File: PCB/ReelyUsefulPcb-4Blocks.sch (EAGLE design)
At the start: 28 parts, among them Q1 200mA/50V, U2 TJCTM240, U3 PHOTON_SMD

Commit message: Updated notes.
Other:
- note added: "Actually photo-transistors (L-93DP3C) Short lead (Collector) goes to +ve"
- note removed: "Diodes need to be reversed"
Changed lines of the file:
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@@
 <wire x1="144.78" y1="2.54" x2="106.68" y2="2.54" width="0.1524" layer="97"/>
 <text x="63.5" y="43.18" size="1.27" layer="97">Hand held detector</text>
-<text x="25.4" y="48.26" size="1.27" layer="91">Diodes need to be reversed</text>
+<text x="25.4" y="48.26" size="1.27" layer="97">Actually photo-transistors (L-93DP3C)
+Short lead (Collector) goes to +ve</text>
 <text x="238.76" y="7.62" size="1.27" layer="97">1.0</text>
 <text x="170.942" y="11.684" size="1.27" layer="97">Stephen Harrison</text>

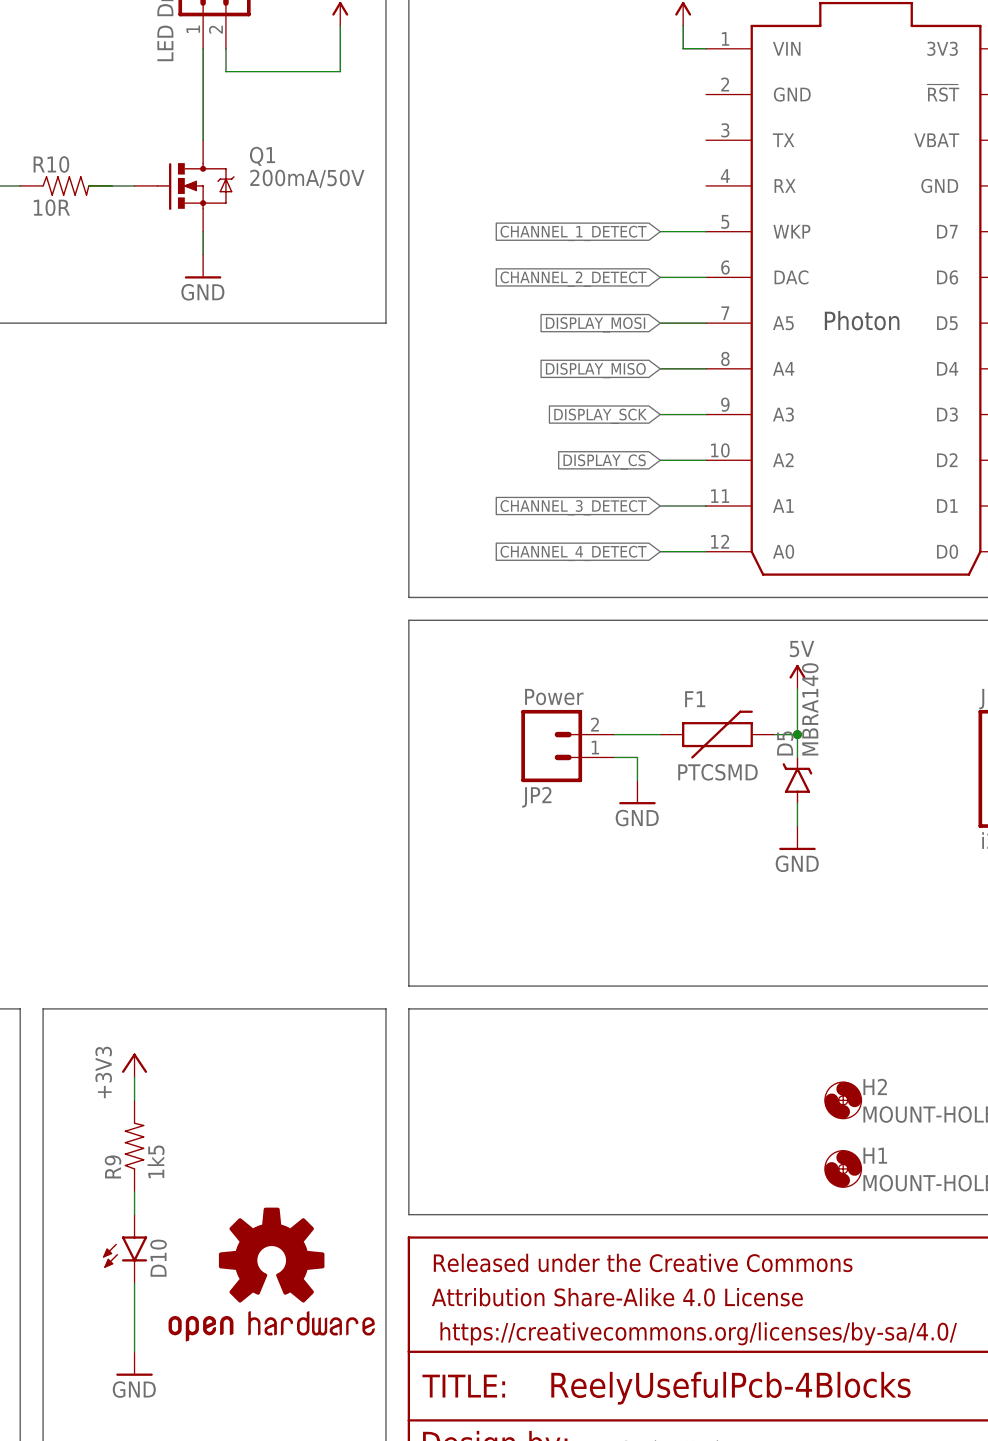
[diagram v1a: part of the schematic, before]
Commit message: Monior improvements to pcb/schematic names and values.
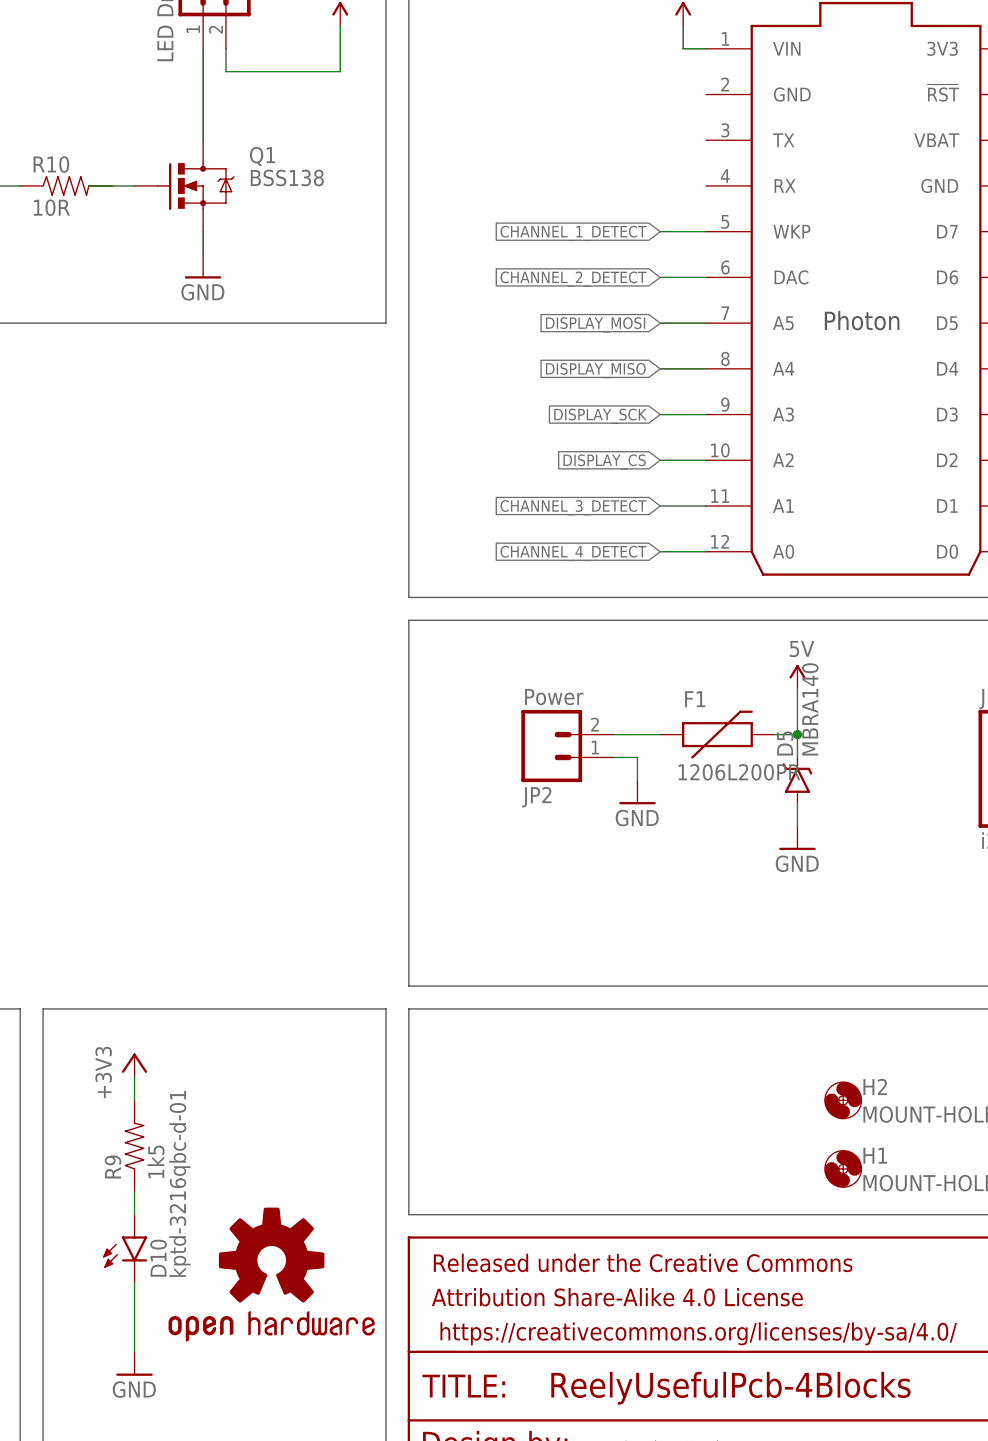
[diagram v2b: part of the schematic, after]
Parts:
- D10: value (none) -> kptd-3216qbc-d-01; FARNELL (none) -> 2290349
- F1: value PTCSMD -> 1206L200PR; FARNELL (none) -> 2383297
- Q1: value 200mA/50V -> BSS138; FARNELL (none) -> 9845330
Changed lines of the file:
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@@
 <part name="FRAME1" library="SparkFun-Aesthetics" deviceset="FRAME-LETTER" device=""/>
 <part name="LOGO1" library="SparkFun-Aesthetics" deviceset="OSHW-LOGO" device="L"/>
-<part name="D10" library="SparkFun-LED" deviceset="LED" device="1206-BOTTOM"/>
+<part name="D10" library="SparkFun-LED" deviceset="LED" device="1206-BOTTOM" value="kptd-3216qbc-d-01">
+<attribute name="FARNELL" value="2290349"/>
+</part>
 <part name="D2" library="SparkFun-LED" deviceset="LED" device="3MM" value="PD204-6C"/>
 <part name="D3" library="SparkFun-LED" deviceset="LED" device="3MM" value="PD204-6C"/>
@@
 <part name="GND10" library="SparkFun-Aesthetics" deviceset="GND" device=""/>
 <part name="JP6" library="SparkFun-Connectors" deviceset="M01" device="PTH"/>
-<part name="Q1" library="SparkFun-DiscreteSemi" deviceset="MOSFET-NCHANNEL" device="BSS138" value="200mA/50V"/>
+<part name="Q1" library="SparkFun-DiscreteSemi" deviceset="MOSFET-NCHANNEL" device="BSS138" value="BSS138">
+<attribute name="FARNELL" value="9845330"/>
+</part>
 <part name="GND12" library="SparkFun-Aesthetics" deviceset="GND" device=""/>
 <part name="R10" library="SparkFun-Resistors" deviceset="RESISTOR" device="1206" value="10R"/>
 <part name="SUPPLY4" library="SparkFun-Aesthetics" deviceset="5V" device=""/>
 <part name="D5" library="SparkFun-DiscreteSemi" deviceset="MBRA140" device=""/>
-<part name="F1" library="SparkFun-PowerIC" deviceset="PTC" device="SMD"/>
+<part name="F1" library="SparkFun-PowerIC" deviceset="PTC" device="SMD" value="1206L200PR">
+<attribute name="FARNELL" value="2383297"/>
+</part>
 <part name="SUPPLY1" library="SparkFun-Aesthetics" deviceset="5V" device=""/>
 <part name="GND14" library="SparkFun-Aesthetics" deviceset="GND" device=""/>
@@
 <instance part="FRAME1" gate="V" x="147.32" y="0"/>
 <instance part="LOGO1" gate="G$1" x="132.08" y="33.02"/>
-<instance part="D10" gate="G$1" x="116.84" y="35.56"/>
+<instance part="D10" gate="G$1" x="116.84" y="35.56">
+<attribute name="FARNELL" x="116.84" y="35.56" size="1.778" layer="96" display="off"/>
+</instance>
 <instance part="D2" gate="G$1" x="15.24" y="38.1" rot="R180"/>
 <instance part="D3" gate="G$1" x="22.86" y="38.1" rot="R180"/>
@@
 <instance part="GND10" gate="1" x="172.72" y="83.82"/>
 <instance part="JP6" gate="G$1" x="228.6" y="142.24" rot="R180"/>
-<instance part="Q1" gate="G$1" x="124.46" y="152.4"/>
+<instance part="Q1" gate="G$1" x="124.46" y="152.4">
+<attribute name="FARNELL" x="124.46" y="152.4" size="1.778" layer="96" display="off"/>
+</instance>
 <instance part="GND12" gate="1" x="124.46" y="142.24"/>
 <instance part="R10" gate="G$1" x="109.22" y="152.4"/>
 <instance part="SUPPLY4" gate="G$1" x="139.7" y="170.18"/>
 <instance part="D5" gate="G$1" x="190.5" y="86.36" rot="R90"/>
-<instance part="F1" gate="G$1" x="180.34" y="91.44"/>
+<instance part="F1" gate="G$1" x="180.34" y="91.44">
+<attribute name="FARNELL" x="180.34" y="91.44" size="1.778" layer="96" display="off"/>
+</instance>
 <instance part="SUPPLY1" gate="G$1" x="190.5" y="96.52"/>
 <instance part="GND14" gate="1" x="190.5" y="78.74"/>
